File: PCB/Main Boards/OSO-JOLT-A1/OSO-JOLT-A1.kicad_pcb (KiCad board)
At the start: 4 copper layers, 27.8 x 28.5 mm, 37 parts, among them J1 OSO_SWD, J2 FH19C-9S-0.5SH_10_, Q1 Q_Photo_NPN, Q2 Q_NMOS_GSD, U1 ATSAML22J18A-MUT, U2 MIC5365-3.3YC5-TR, U3 SENSOR-WATCH-JOLT-USB, X1 Crystal

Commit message: Laying out components
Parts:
- removed Q1: Q_Photo_NPN, Resistor_SMD:R_0603_1608Metric
- removed R1: 10K, Resistor_SMD:R_0201_0603Metric
- removed R6: 1K, Resistor_SMD:R_0603_1608Metric
- removed R7: 100, Resistor_SMD:R_0603_1608Metric
- C2: moved to F.Cu
- L2: moved to B.Cu
- moved RESET0 16.9 mm to (145.6, 102.0)
- moved TP10 16.9 mm to (173.3, 92.8)
- moved C2 13.9 mm to (150.6, 98.6), turned to 90 degrees
- moved L1 13.9 mm to (144.5, 118.8), turned to 0 degrees
- moved U2 12.4 mm to (163.3, 108.8)
- moved J2 11.6 mm to (163.4, 98.2), turned to -90 degrees
- moved C1 10.3 mm to (177.9, 98.7)
- moved D1 10.0 mm to (166.3, 108.8), turned to -90 degrees
- moved R10 9.66 mm to (152.1, 110.5), turned to 0 degrees
- moved TP11 7.79 mm to (167.5, 105.9)
- moved R11 7.64 mm to (150.4, 107.3)
- moved L2 7.44 mm to (158.4, 113.7)
- moved R2 5.33 mm to (151.8, 107.9)
- moved Q2 2.99 mm to (151.8, 109.4), turned to -90 degrees
- moved R8 1.69 mm to (148.6, 98.7)
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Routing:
- net GND: track 58.7 -> 0.00 mm, vias 14 -> 0
- net /COM0: track 28.5 -> 0.00 mm
- net /COM1: track 26.6 -> 0.00 mm
- net VCC: track 25.5 -> 0.00 mm, vias 12 -> 0
- net /LIGHTSENSE: track 24.8 -> 0.00 mm, vias 3 -> 0
- net /COM2: track 24.8 -> 0.00 mm
- net /~{RESET}: track 21.9 -> 0.00 mm, vias 2 -> 0
- net (no net): track 21.6 -> 0.00 mm, vias 4 -> 0
- net /ADJUST: track 20.6 -> 0.00 mm, vias 1 -> 0
- net /SWCLK_LIGHT: track 20.4 -> 0.00 mm, vias 2 -> 0
- net /SWDIO_MODE: track 18.8 -> 0.00 mm, vias 2 -> 0
- net VBUS: track 17.6 -> 0.00 mm, vias 2 -> 0
- net /USB_P: track 16.6 -> 0.00 mm, vias 2 -> 0
- net /USB_N: track 15.9 -> 0.00 mm, vias 2 -> 0
- net /VLCD: track 14.3 -> 0.00 mm, vias 3 -> 0
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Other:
- outline, holes or cut-outs redrawn
- board text added: "Sensor Watch Jolt!"
- board text added: "v1.0.0"
- board text removed: "SWAT-C1-06"
- board text removed: "Sensor Watch Pro!"

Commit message: Pre-routing commit
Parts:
- removed G***: LOGO, LOGO
- L1: moved to B.Cu
- Q2, R2, R3, R4: moved to F.Cu
- moved C1 16.1 mm to (161.9, 99.8), turned to 90 degrees
- moved TP1 14.0 mm to (148.2, 93.8)
- moved L1 9.64 mm to (148.2, 110.0), turned to 90 degrees
- moved TP8 8.37 mm to (148.2, 96.5)
- moved TP10 7.34 mm to (166.1, 93.5)
- moved Q2 6.45 mm to (158.2, 109.8), turned to 0 degrees
- moved TP11 6.24 mm to (164.7, 111.5)
- moved R3 6.07 mm to (156.9, 107.9), turned to 0 degrees
- moved R4 6.03 mm to (156.9, 107.2)
- moved R2 4.95 mm to (156.4, 109.6), turned to -90 degrees
- moved TP9 3.28 mm to (148.0, 110.8)
- moved C5 1.83 mm to (154.3, 109.0)
- moved R10 1.66 mm to (151.3, 109.0), turned to 180 degrees
- moved R11 0.76 mm to (151.2, 107.5)
- moved J2 0.20 mm to (163.6, 98.2)
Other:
- board text added: "by devolov"
- board text removed: "9-Pin connector:"
- board text removed: "A0: PB04 SDA: PB30/SERCOM1.0 SCL: PB31/SERCOM1.1 A1/SCK:PB01/TC3.1/S3.3 A2/MOSI:PB02/TC2.0/S3.0 A3/CS: PB03/TC2.1 A4/MISO: PB00/TC3.0 /S3.2"
- board text removed: "Alarm btn: PA02/ I2/ RTC. IN2"
- board text removed: "CC-BY-SA 4.0"
- board text removed: "Light + Sound: ~Red: PA12/TCC.6 ~Blue: PA13/TCC.7 ~Green: PA22/TCC.4 Piezo: PA27/TCC.5"
- board text removed: "Light Btn: PA30/I10 Temp Sense: PA03 TS ~Enable: PB23 Light Sense: PA04 LS ~Enable: PB22"
- board text removed: "Mode Btn: PA31/I11"
- board text removed: "by joey castillo"

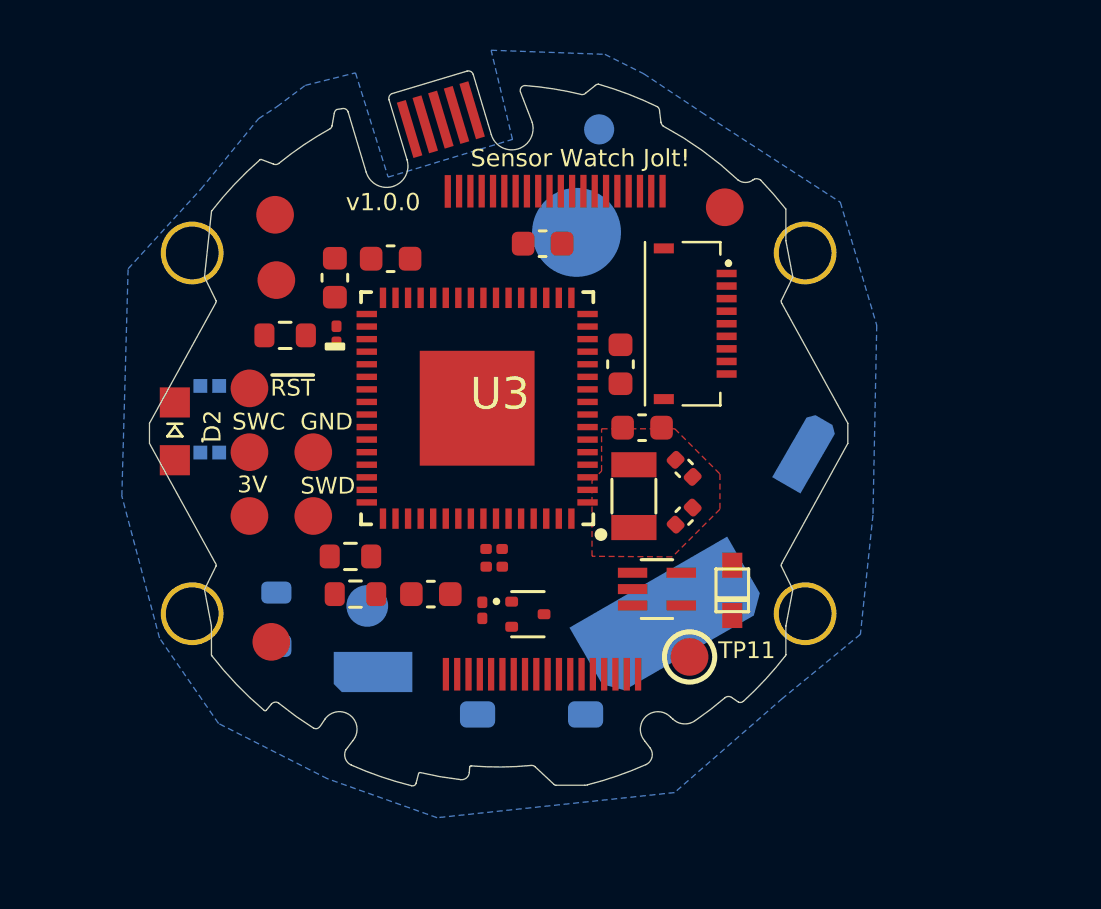
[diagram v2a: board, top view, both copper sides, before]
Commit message: Began routing and added courtyard for light bracket
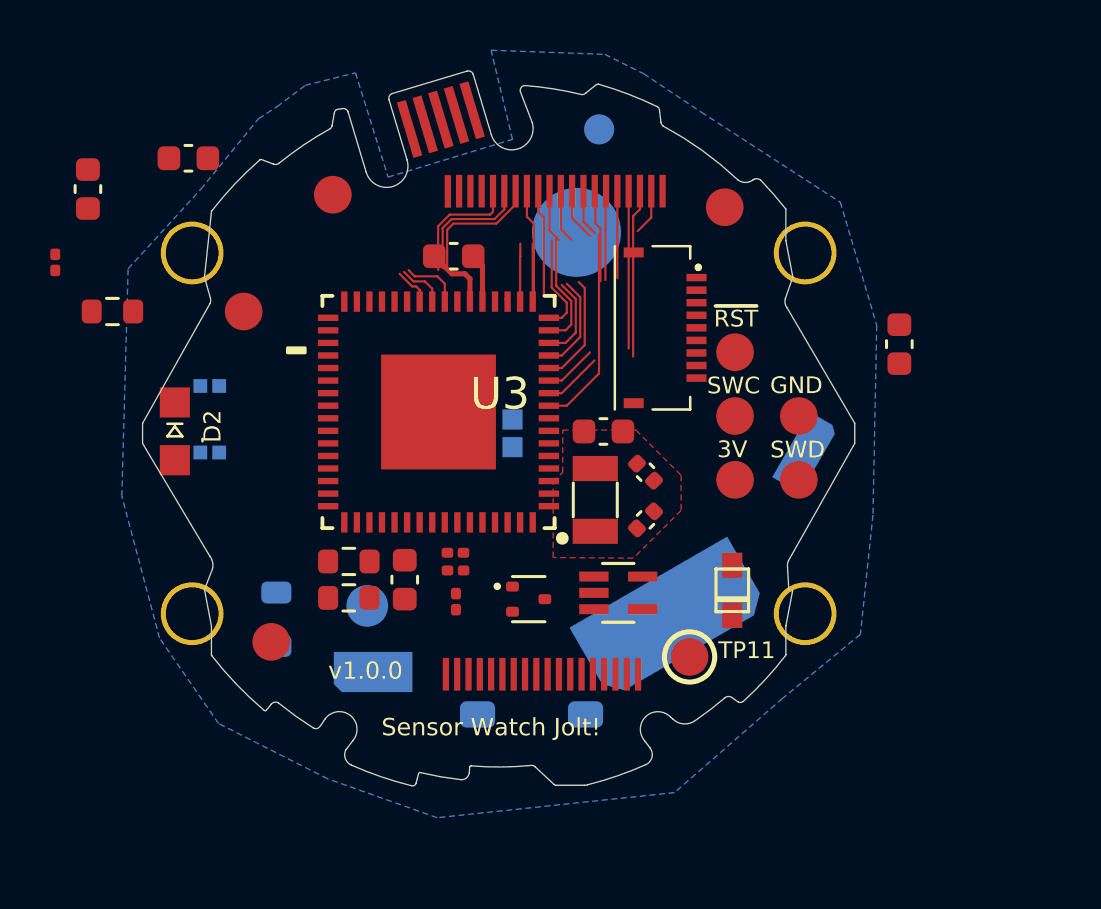
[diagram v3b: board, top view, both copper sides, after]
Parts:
- added ?: , clipboard:c115609c-3c0c-41ab-b51f-504fcf989f35, F.Cu at (188.0, 106.7)
- added ?: , clipboard:8bda33a4-6256-413a-81cc-348e83334dcd, F.Cu at (179.0, 106.9)
- added ?: , clipboard:8bda33a4-6256-413a-81cc-348e83334dcd, F.Cu at (184.2, 118.6)
- added ?: , clipboard:95a06284-08e4-4c85-800c-3e27c7f1ff86, F.Cu at (145.1, 116.0)
- moved J1 19.4 mm to (167.7, 101.9)
- moved C2 11.6 mm to (139.4, 95.7)
- moved C1 11.1 mm to (173.0, 99.0)
- moved C3 10.4 mm to (140.7, 92.8)
- moved C6 8.99 mm to (144.7, 91.6)
- moved R8 6.94 mm to (141.7, 97.7)
- moved C4 3.57 mm to (155.3, 95.5), turned to 180 degrees
- moved TP1 2.44 mm to (150.4, 93.0)
- moved TP8 1.80 mm to (146.9, 97.7)
- moved R4 1.55 mm to (155.3, 107.3), turned to 0 degrees
- moved C8 1.55 mm to (162.9, 104.1)
- moved R3 1.55 mm to (155.3, 108.0)
- moved U1 1.55 mm to (154.7, 101.7)
- moved U2 1.55 mm to (161.8, 108.9)
- moved X1 1.55 mm to (160.9, 105.2)
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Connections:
- U1 pad 12: /SEG0 -> /COM3
- U1 pad 13: /COM3 -> /SEG0
- U2 pad 4: (no net) -> unconnected-(U2-NC-Pad4)
- U3 pad A16: /COM0 -> /COM3
- U3 pad A17: /COM1 -> /COM2
- U3 pad A18: /COM2 -> /COM1
- U3 pad A19: /COM3 -> /COM0
- U3 pad ADJUST: (no net) -> /ADJUST
- U3 pad B10: /SEG19 -> /SEG16
- U3 pad B11: /SEG18 -> /SEG17
- U3 pad B12: /SEG17 -> /SEG18
- U3 pad B13: /SEG15 -> /SEG19
- U3 pad B14: (no net) -> /SEG20
- U3 pad B15: /SEG14 -> /SEG21
- U3 pad B16: /SEG13 -> /SEG22
- U3 pad B17: /SEG12 -> /SEG26
- U3 pad B18: /SEG11 -> /SEG23
- U3 pad B3: /SEG26 -> /SEG12
- U3 pad B4: /SEG25 -> /SEG11
- U3 pad B5: /SEG24 -> /SEG25
- U3 pad B6: /SEG23 -> /SEG24
- U3 pad B7: /SEG22 -> /SEG13
- U3 pad B8: /SEG21 -> /SEG14
- U3 pad B9: /SEG20 -> /SEG15
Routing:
- net /COM0: track 0.00 -> 9.86 mm
- net /COM1: track 0.00 -> 9.05 mm
- net /COM2: track 0.00 -> 8.37 mm
- net /COM3: track 0.00 -> 7.88 mm
- net /SEG8: track 0.00 -> 7.50 mm
- net /SEG0: track 0.00 -> 7.44 mm
- net /SEG1: track 0.00 -> 7.04 mm
- net /SEG9: track 0.00 -> 6.99 mm
- net /SEG2: track 0.00 -> 6.58 mm
- net /SEG10: track 0.00 -> 6.52 mm
- net /SEG3: track 0.00 -> 6.03 mm
- net /SEG4: track 0.00 -> 4.42 mm
- net /SEG5: track 0.00 -> 4.40 mm
- net /SEG6: track 0.00 -> 4.38 mm
- net /SEG7: track 0.00 -> 4.36 mm
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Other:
- board size 27.8 x 28.5 mm -> 28.3 x 28.5 mm

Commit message: Seperate DW5600 components and made the edge cuts live on thepcb
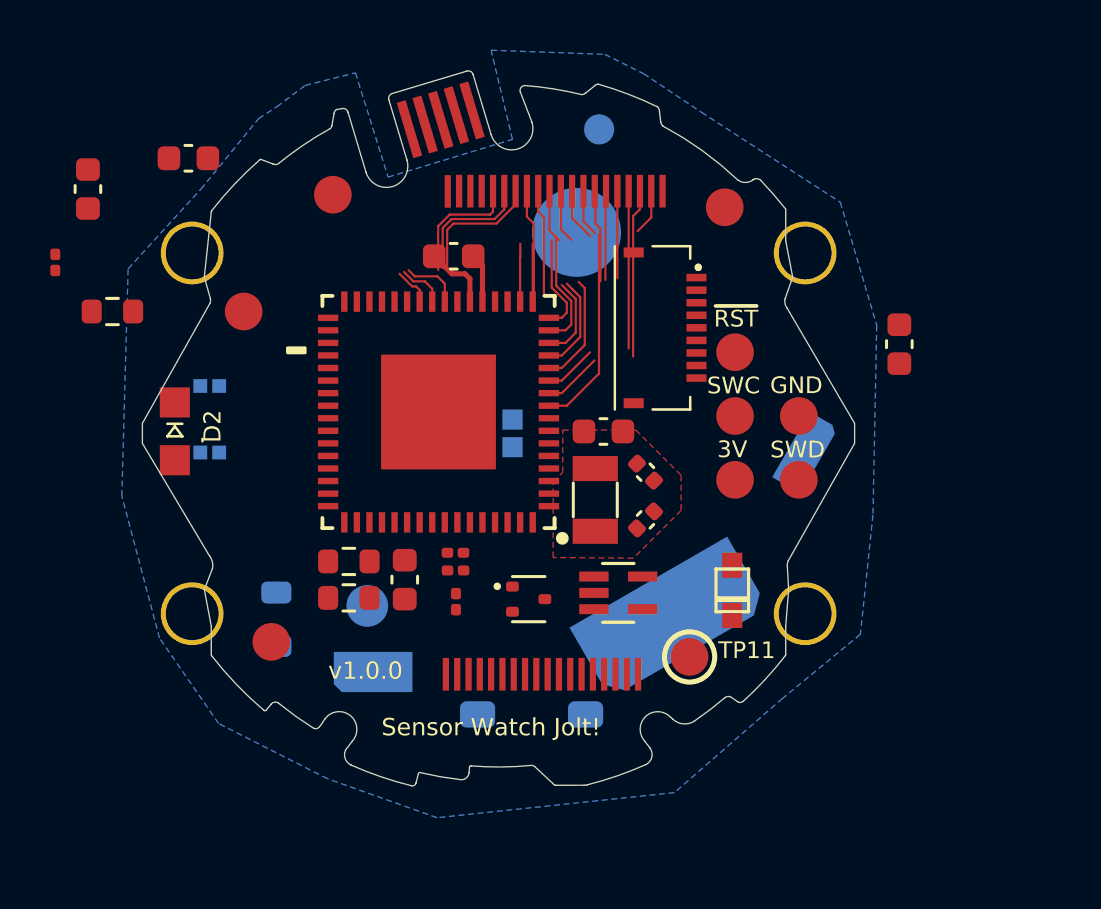
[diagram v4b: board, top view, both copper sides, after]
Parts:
- removed ?: , clipboard:c115609c-3c0c-41ab-b51f-504fcf989f35
- removed ? (x2): , clipboard:8bda33a4-6256-413a-81cc-348e83334dcd
- removed ?: , clipboard:95a06284-08e4-4c85-800c-3e27c7f1ff86
- removed U3: SENSOR-WATCH-JOLT-USB, OSO-SWAT-A1-05:CASIO-DW5600-OUTLINE-USB
- added SW1: ~, OSO-SWAT-A1-05:CASIO-DW5600-BTN, F.Cu at (144.8, 95.4)
- added SW2: ~, OSO-SWAT-A1-05:CASIO-DW5600-BTN, F.Cu at (144.8, 109.7)
- added SW3: ~, OSO-SWAT-A1-05:CASIO-DW5600-BTN, F.Cu at (169.2, 95.4)
- added SW4: ~, OSO-SWAT-A1-05:CASIO-DW5600-BTN, F.Cu at (169.2, 109.7)
- added U4: ~, OSO-SWAT-A1-05:CASIO-DW5600-PWR-BUZZER, F.Cu at (157.1, 102.5)
- added U5: ~, OSO-SWAT-A1-05:CASIO-DW5600-USB, F.Cu at (154.7, 90.1)
- added U6: ~, OSO-SWAT-A1-05:CASIO-DW5600-LCD, F.Cu at (157.1, 102.5)
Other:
- outline, holes or cut-outs redrawn

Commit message: Resynced pcb and sch
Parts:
- removed Q2: Q_NMOS_GSD, Package_TO_SOT_SMD:SOT-523
- removed R10: 10K THERM, Resistor_SMD:R_0603_1608Metric
- removed R11: 10K 0.1%, Resistor_SMD:R_0603_1608Metric
- removed R8: 100, Resistor_SMD:R_0603_1608Metric
- removed RESET0: EVP-BB1AAB000, OSO-SWAT-A1-05:SW_EVP-BB1AAB000
- removed TP10, TP11, TP8, TP9: MICROBUILDER_TESTPOINTROUND1.5MM, OSO-SWAT-A1-05:MICROBUILDER_TESTPOINT_ROUND_1.5MM
- removed U6: ~, OSO-SWAT-A1-05:CASIO-DW5600-LCD
- added Q1: Q_NMOS_GSD, Package_TO_SOT_SMD:SOT-523, F.Cu at (158.2, 109.2)
- added R1: 10K, Resistor_SMD:R_0201_0603Metric, F.Cu at (155.3, 109.2)
- added R5: 10K THERM, Resistor_SMD:R_0603_1608Metric, F.Cu at (151.1, 109.1)
- added R6: 10K 0.1%, Resistor_SMD:R_0603_1608Metric, F.Cu at (151.1, 107.7)
- added RESET1: EVP-BB1AAB000, OSO-SWAT-A1-05:SW_EVP-BB1AAB000, B.Cu at (145.6, 102.0)
- added TP2: MICROBUILDER_TESTPOINTROUND1.5MM, OSO-SWAT-A1-05:MICROBUILDER_TESTPOINT_ROUND_1.5MM, F.Cu at (144.8, 95.4)
- added TP3: MICROBUILDER_TESTPOINTROUND1.5MM, OSO-SWAT-A1-05:MICROBUILDER_TESTPOINT_ROUND_1.5MM, F.Cu at (144.8, 109.7)
- added TP4: MICROBUILDER_TESTPOINTROUND1.5MM, OSO-SWAT-A1-05:MICROBUILDER_TESTPOINT_ROUND_1.5MM, F.Cu at (169.2, 95.4)
- added TP5: MICROBUILDER_TESTPOINTROUND1.5MM, OSO-SWAT-A1-05:MICROBUILDER_TESTPOINT_ROUND_1.5MM, F.Cu at (169.2, 109.7)
- added U3: ~, OSO-SWAT-A1-05:CASIO-DW5600-USB, F.Cu at (154.7, 90.1)
- C1: value 10uF -> 1uF; moved to B.Cu
- C2: footprint Capacitor_SMD:C_0201_0603Metric -> Capacitor_SMD:C_0603_1608Metric
- C3: footprint Capacitor_SMD:C_0603_1608Metric -> Capacitor_SMD:C_0201_0603Metric
- C5: value 1uF -> 10uF
- C7: value 22pf -> 1uF; footprint Capacitor_SMD:C_0402_1005Metric -> Capacitor_SMD:C_0603_1608Metric
- C9: value 1uF -> 22pf; footprint Capacitor_SMD:C_0603_1608Metric -> Capacitor_SMD:C_0402_1005Metric
- R2: value 10K -> 100; footprint Resistor_SMD:R_0201_0603Metric -> Resistor_SMD:R_0603_1608Metric
- U2: value MIC5365-3.3YC5-TR -> ~; footprint OSO-SWAT-A1-05:SOT65P210X110-5N -> OSO-SWAT-A1-05:CASIO-DW5600-PWR-BUZZER
- U4: value ~ -> MIC5365-3.3YC5-TR; footprint OSO-SWAT-A1-05:CASIO-DW5600-PWR-BUZZER -> OSO-SWAT-A1-05:SOT65P210X110-5N
- U5: footprint OSO-SWAT-A1-05:CASIO-DW5600-USB -> OSO-SWAT-A1-05:CASIO-DW5600-LCD
- moved C1 26.1 mm to (148.1, 106.7), turned to 0 degrees
- moved C2 17.7 mm to (157.1, 95.5)
- moved U5 12.7 mm to (157.1, 102.5)
- moved C3 9.36 mm to (148.8, 97.5)
- moved C6 8.29 mm to (152.0, 95.5)
- moved U2 7.94 mm to (157.1, 102.5)
- moved R2 7.81 mm to (148.0, 106.5), turned to 180 degrees
- moved L1 0.15 mm to (148.2, 109.8), turned to -90 degrees
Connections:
- C1 pad 1: VCC -> /VDDCORE
- C5 pad 1: /VDDCORE -> VCC
- C7 pad 1: /XIN32 -> +3V3
- C9 pad 1: +3V3 -> /XIN32
- R2 pad 1: /BUZZER -> /~{LED}
- R2 pad 2: GND -> Net-(D2-C)
- R3 pad 2: /SCL -> /SDA
- R4 pad 2: /SDA -> /SCL
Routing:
- net /COM0: track 9.86 -> 0.00 mm
- net /COM1: track 9.05 -> 0.00 mm
- net /COM2: track 8.37 -> 0.00 mm
- net /COM3: track 7.88 -> 0.00 mm
- net /SEG8: track 7.50 -> 0.00 mm
- net /SEG0: track 7.44 -> 0.00 mm
- net /SEG1: track 7.04 -> 0.00 mm
- net /SEG9: track 6.99 -> 0.00 mm
- net /SEG2: track 6.58 -> 0.00 mm
- net /SEG10: track 6.52 -> 0.00 mm
- net /SEG3: track 6.03 -> 0.00 mm
- net /SEG4: track 4.42 -> 0.00 mm
- net /SEG5: track 4.40 -> 0.00 mm
- net /SEG6: track 4.38 -> 0.00 mm
- net /SEG7: track 4.36 -> 0.00 mm
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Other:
- outline, holes or cut-outs redrawn
- board text removed: "EXTEND GND POUR IF MANUFACTURING AT 0.6mm THICKNESS"

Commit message: end of day routing commit
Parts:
- R2: moved to B.Cu
- moved Q1 16.9 mm to (142.4, 115.1)
- moved C4 13.1 mm to (151.0, 107.9), turned to 0 degrees
- moved C5 12.4 mm to (165.5, 106.3), turned to 0 degrees
- moved R3 10.8 mm to (164.8, 103.0)
- moved R5 10.2 mm to (161.2, 110.5), turned to 0 degrees
- moved R6 10.2 mm to (161.2, 109.0)
- moved R4 10.2 mm to (164.9, 103.7)
- moved U4 9.72 mm to (164.0, 109.4), turned to -90 degrees
- moved R2 8.79 mm to (147.8, 97.7), turned to -105 degrees
- moved C9 3.90 mm to (162.9, 106.0), turned to 45 degrees
- moved C7 3.67 mm to (161.8, 102.5), turned to 0 degrees
- moved R1 2.72 mm to (153.0, 107.9)
- moved TP1 1.35 mm to (149.1, 93.2)
- moved C3 0.81 mm to (149.1, 98.2)
- moved C6 0.81 mm to (152.2, 94.7), turned to 0 degrees
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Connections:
- U4 pad 4: (no net) -> unconnected-(U4-NC-Pad4)
- U5 pad B10: /SEG16 -> /SEG23
- U5 pad B11: /SEG17 -> /SEG16
- U5 pad B12: /SEG18 -> /SEG15
- U5 pad B13: /SEG19 -> /SEG14
- U5 pad B14: /SEG20 -> /SEG13
- U5 pad B15: /SEG21 -> /SEG25
- U5 pad B16: /SEG22 -> /SEG24
- U5 pad B17: /SEG26 -> /SEG12
- U5 pad B18: /SEG23 -> /SEG11
- U5 pad B3: /SEG12 -> /SEG17
- U5 pad B4: /SEG11 -> /SEG18
- U5 pad B5: /SEG25 -> /SEG19
- U5 pad B6: /SEG24 -> /SEG20
- U5 pad B7: /SEG13 -> /SEG21
- U5 pad B8: /SEG14 -> /SEG22
- U5 pad B9: /SEG15 -> /SEG26
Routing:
- net /SEG11: track 0.00 -> 40.3 mm
- net /SEG12: track 0.00 -> 38.7 mm
- net /SEG24: track 0.00 -> 37.3 mm
- net /SEG25: track 0.00 -> 35.5 mm
- net /SEG13: track 0.00 -> 33.9 mm
- net /SEG14: track 0.00 -> 31.6 mm
- net /SEG15: track 0.00 -> 27.0 mm
- net /SEG16: track 0.00 -> 25.5 mm
- net /SEG17: track 0.00 -> 20.4 mm
- net /SEG18: track 0.00 -> 19.9 mm
- net /SEG19: track 0.00 -> 19.5 mm
- net /SEG21: track 0.00 -> 19.3 mm
- net /SEG20: track 0.00 -> 19.1 mm
- net /SEG22: track 0.00 -> 18.9 mm
- net /SEG26: track 0.00 -> 18.6 mm
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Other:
- outline, holes or cut-outs redrawn
